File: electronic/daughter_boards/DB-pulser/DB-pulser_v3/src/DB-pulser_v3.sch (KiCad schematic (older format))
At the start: 16 parts, among them P1 CONN_01X19, P2 SMA, P3 CONN_01X02, P4 SMA, P5 SMA, P6 CONN_01X02, P7 CONN_01X02, U1 MOSFET_driver, U2 TC6320

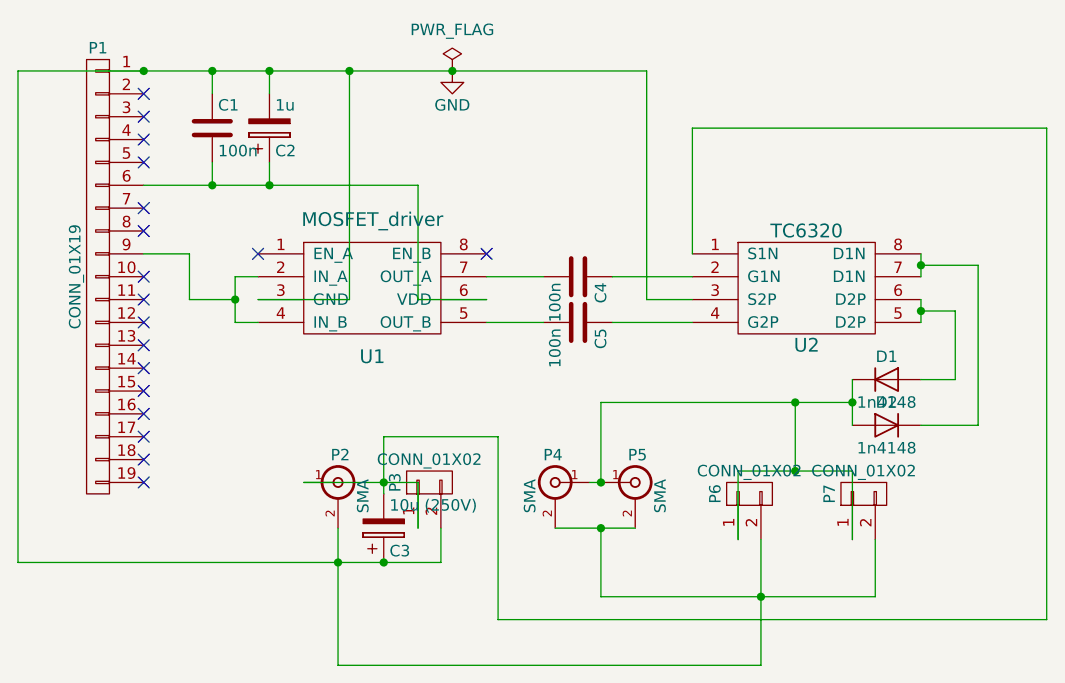
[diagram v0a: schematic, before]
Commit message: update pulser ref
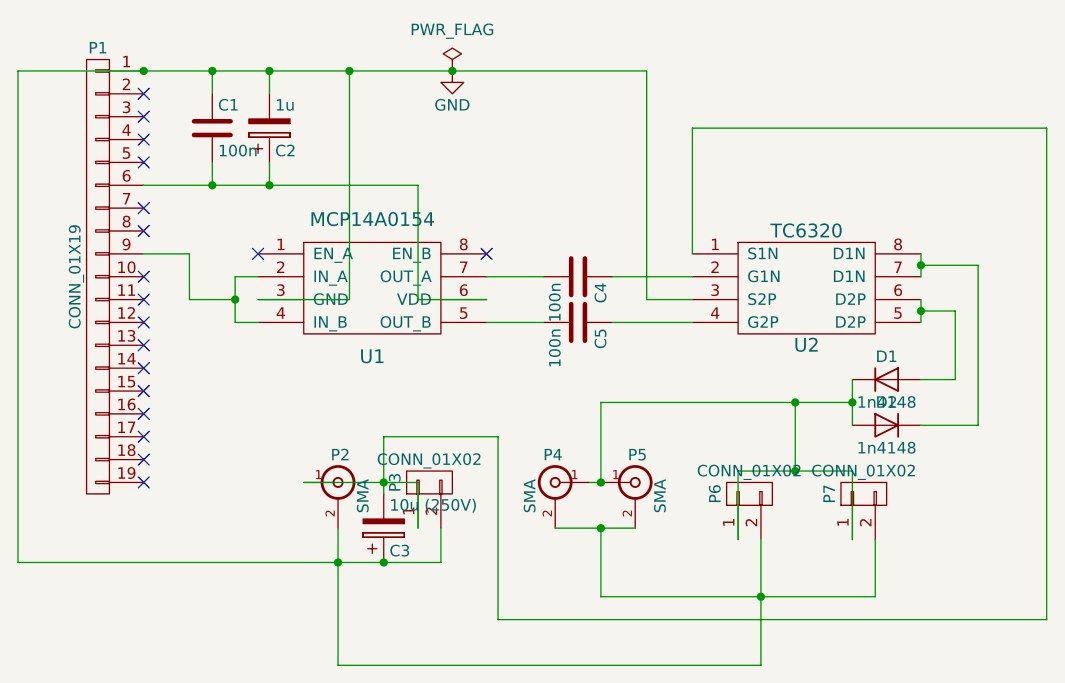
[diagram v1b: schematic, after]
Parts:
- U1: value MOSFET_driver -> MCP14A0154
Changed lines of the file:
@@
 P 4450 3700
 F 0 "U1" H 4450 3400 60  0000 C CNN
-F 1 "MOSFET_driver" H 4450 4000 60  0000 C CNN
+F 1 "MCP14A0154" H 4450 4000 60  0000 C CNN
 F 2 "Echopen:MSOP-8" H 4450 3650 60  0001 C CNN
 F 3 "" H 4450 3650 60  0001 C CNN

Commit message: update instalation doc
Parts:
- added R1: 47, Echopen:Resistor_TH_common, symbol R
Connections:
- net GND: now also R1.2
- net at D1.1 (K), D2.2 (A), P4.1 (In)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: now also R1.1
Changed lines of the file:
@@
 Wire Wire Line
 	6150 5350 4300 5350
+$Comp
+L R R1
+U 1 1 59D64A31
+P 5800 4350
+F 0 "R1" V 5880 4350 50  0000 C CNN
+F 1 "47" V 5800 4350 50  0000 C CNN
+F 2 "Echopen:Resistor_TH_common" V 5730 4350 50  0001 C CNN
+F 3 "" H 5800 4350 50  0001 C CNN
+	1    5800 4350
+	1    0    0    -1
+$EndComp
+Connection ~ 5800 4200
+Wire Wire Line
+	5800 4500 5800 5050
+Connection ~ 5800 5050
 $EndSCHEMATC
